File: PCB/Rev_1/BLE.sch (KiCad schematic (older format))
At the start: 14 parts, among them J4 WURTH_61300411121, J5 FTSH-105-01-F-DV-K

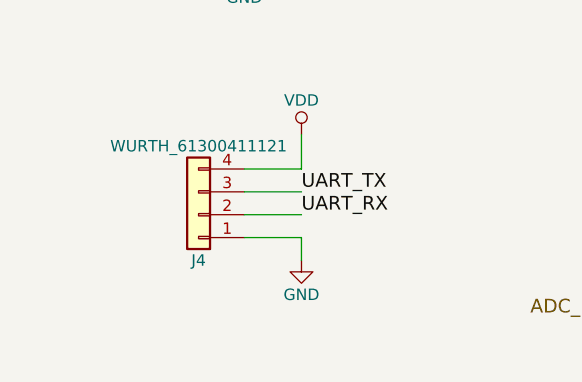
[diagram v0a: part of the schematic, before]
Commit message: UART header not fitted
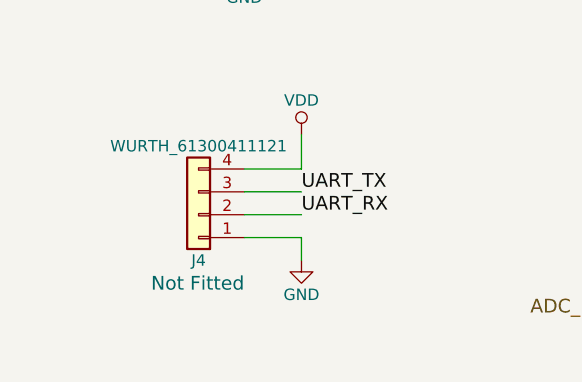
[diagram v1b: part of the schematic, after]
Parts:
- J4: Assembly Option Fitted -> Not Fitted
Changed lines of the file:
@@
 F 10 "https://www.digikey.com/product-detail/en/wurth-electronics-inc/61300411121/732-5317-ND/4846827" H 1325 5250 60  0001 L CNN "Supplier Link"
 F 11 "4 Positions Header Connector 0.100 (2.54mm) Through Hole Gold" H 1325 5350 60  0001 L CNN "Description"
-F 12 "Fitted" H 1325 5450 60  0001 L CNN "Assembly Option"
+F 12 "Not Fitted" H 1100 4550 60  0000 L CNN "Assembly Option"
 	1    1300 4250
 	-1   0    0    1
